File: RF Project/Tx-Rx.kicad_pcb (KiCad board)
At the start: 2 copper layers, 30 x 55 mm, 26 parts, among them J1 CONN_Right, J2 CONN_Left, U1 CC2500RGPR, U2 U.FL_male

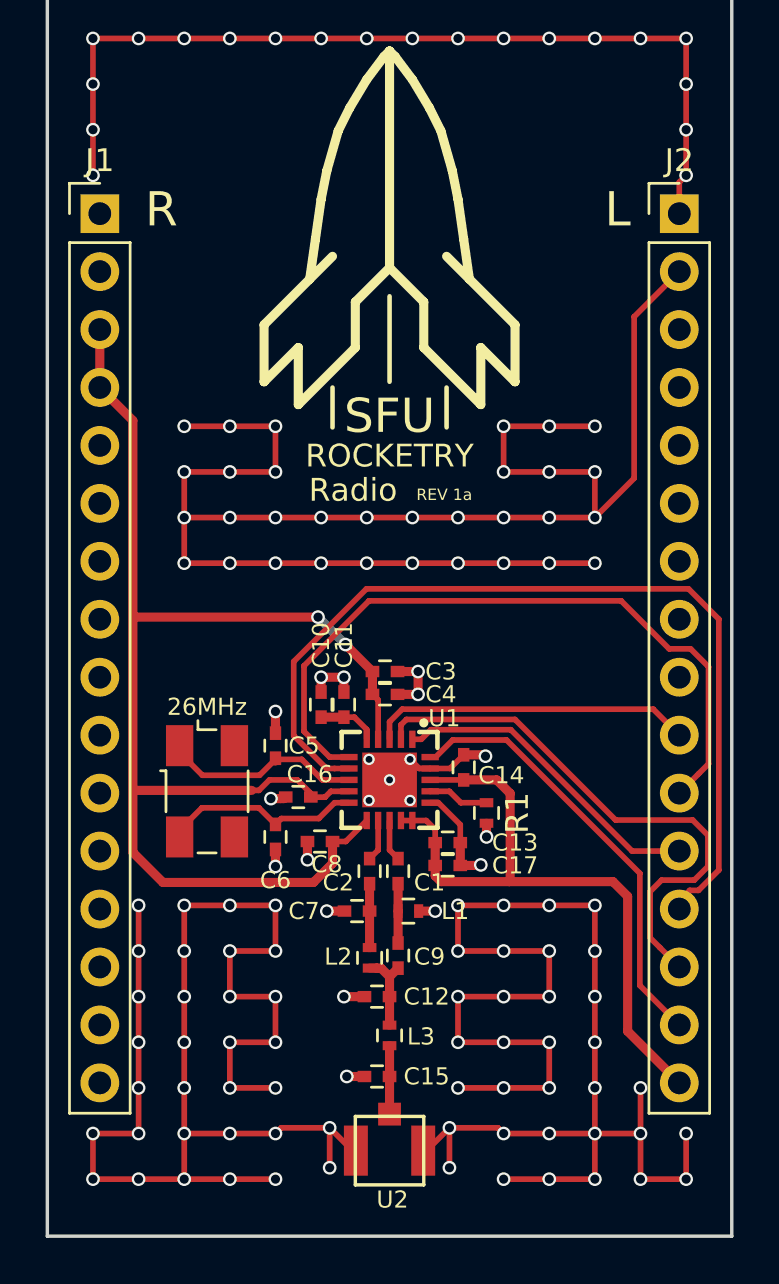
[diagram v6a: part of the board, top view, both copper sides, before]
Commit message: shifted the headers down by 3.77mm since Harrisons board is centered at 102.5mm not 100mm and I thought 15/2 was 8 (woops). Still haven't swapped left with right, that would take too long :P
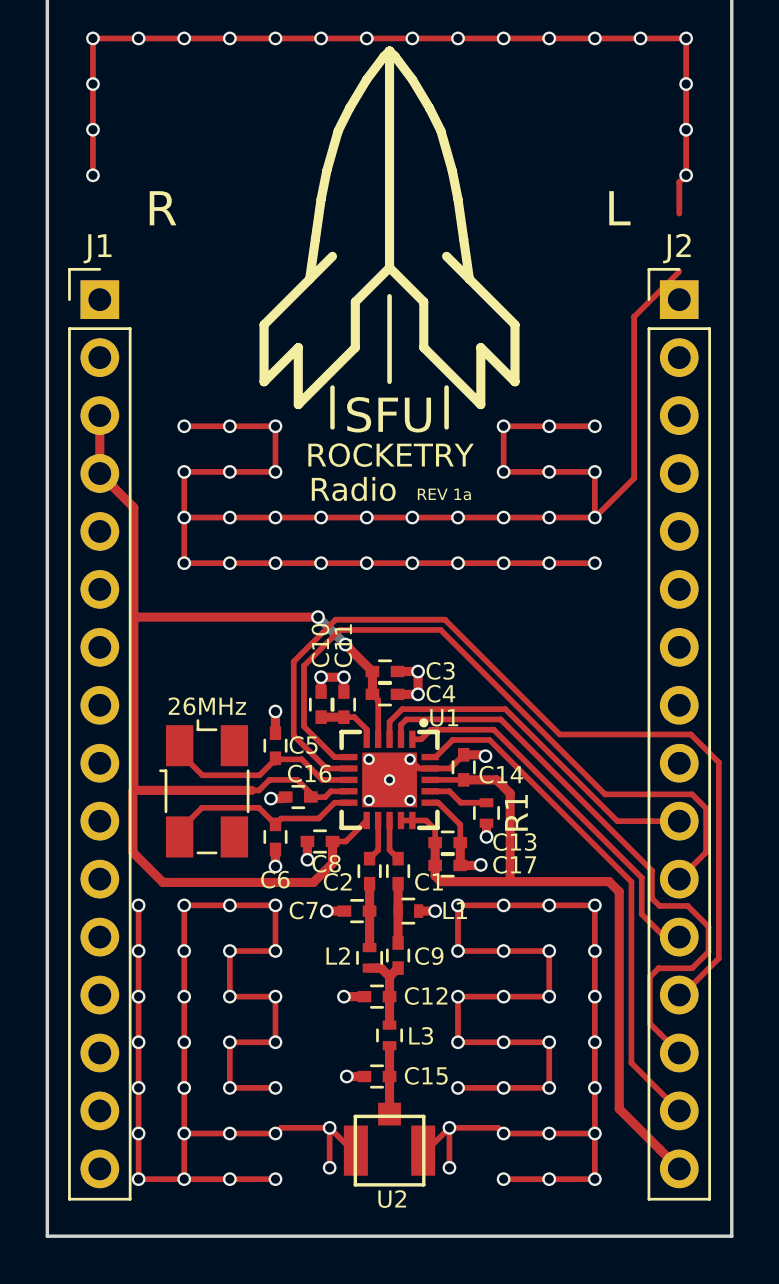
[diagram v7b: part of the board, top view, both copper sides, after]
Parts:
- moved J1 3.77 mm to (87.3, 86.5)
- moved J2 3.77 mm to (112.7, 86.5)
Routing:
- net PWR_GND: track 273.0 -> 259.0 mm, vias 137 -> 130
- net PD3/SI: track 19.3 -> 22.6 mm
- net PD2/SO(GDO1): track 24.5 -> 26.7 mm
- net PD0/SCLK: track 14.6 -> 16.6 mm
- net PE5/GDO0: track 32.0 -> 30.3 mm
- net PE4/GD02: track 14.2 -> 15.7 mm
- net PD1/CSn: track 40.4 -> 39.2 mm

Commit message: Fixed stuff and hopefully non gitbash people will actually be able to download and see this..
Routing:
- net PWR_GND: track 259.0 -> 310.6 mm, vias 130 -> 156
